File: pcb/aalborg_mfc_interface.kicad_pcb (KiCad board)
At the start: 2 copper layers, 118.1 x 54.6 mm, 27 parts, among them J1 DB15FV, J2 DB15FV, J3 DB15FV, P1 PWR_JACK_2.5x5.5, P2 HEADER_01X03, P3 HEADER_01X03, P4 HEADER_01X03, P5 HEADER_01X03, SW1 SPST_SERIES_M, U1 MAX6817

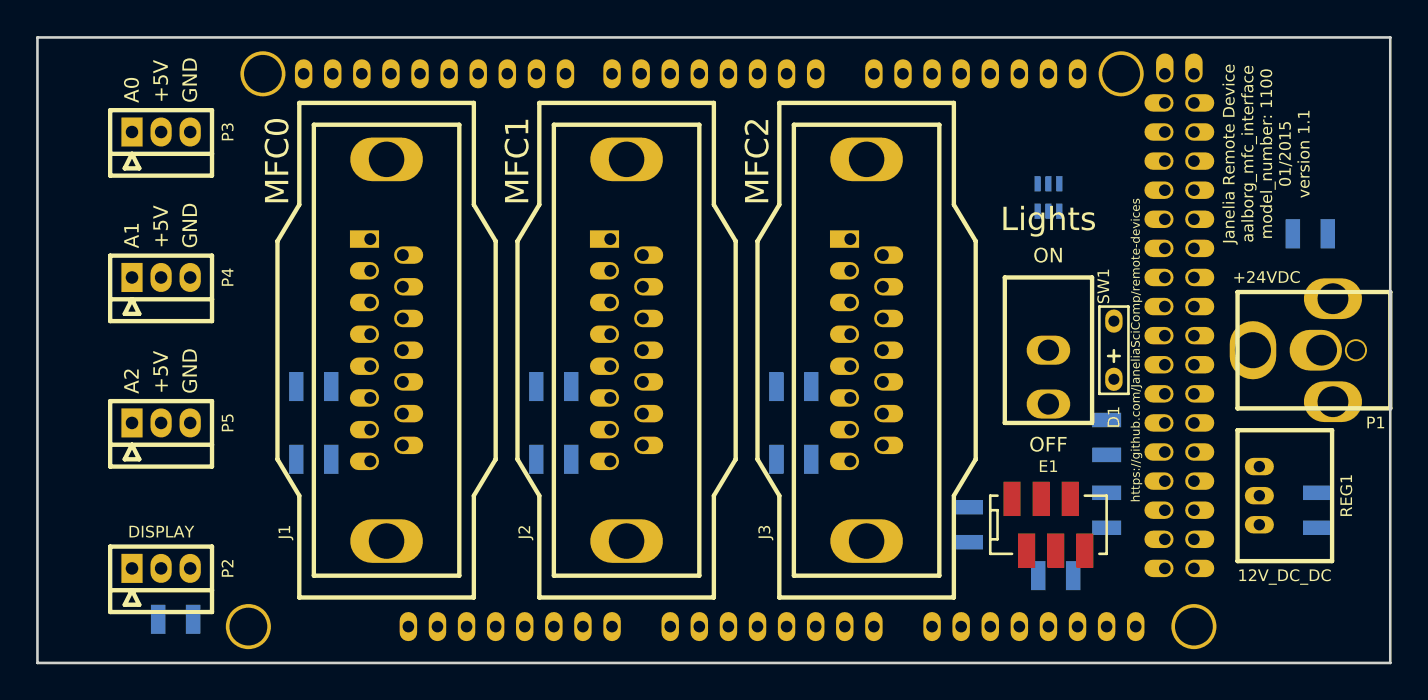
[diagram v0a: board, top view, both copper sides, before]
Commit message: Progress on pcb 1.1 design and firmware 1.0.
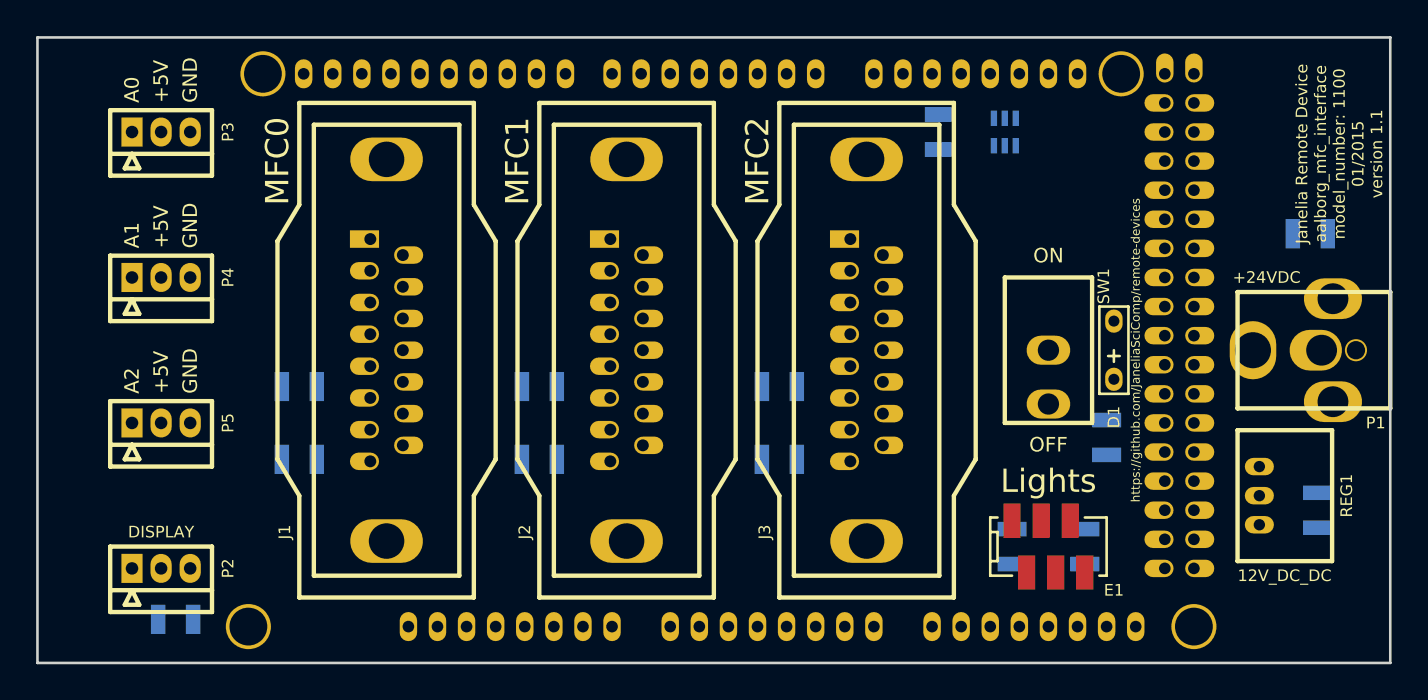
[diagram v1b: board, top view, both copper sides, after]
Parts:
- moved C4 40.0 mm to (172.1, 83.8), turned to 270 degrees
- moved U1 6.87 mm to (177.8, 83.8)
- moved R2 4.26 mm to (178.4, 120.0)
- moved R1 3.70 mm to (184.8, 120.0)
- moved E1 1.91 mm to (181.6, 120.0)
- moved C6 1.27 mm to (137.2, 106.0)
- moved R5 1.27 mm to (137.2, 112.4)
- moved C5 1.27 mm to (116.2, 106.0)
- moved R4 1.27 mm to (116.2, 112.4)
- moved C7 1.27 mm to (158.1, 106.0)
- moved R6 1.27 mm to (158.1, 112.4)
- turned R3 to 270 degrees

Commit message: Progress towards pcb v1.1.
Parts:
- added C8: 10uF, aalborg_mfc_interface:SM1210, B.Cu at (158.1, 106.0)
- added S1: HEADER_01X02, aalborg_mfc_interface:Header_Shrouded_2_Pin, F.Cu at (184.2, 88.3)
- added SW2: KT_SWITCH, aalborg_mfc_interface:KT_SWITCH, F.Cu at (200.0, 88.3)
- added U2: MAX6817, aalborg_mfc_interface:MAX6817, B.Cu at (182.9, 83.2)
- C5: value 10uF -> 0.1uF
- P2: footprint aalborg_mfc_interface:Header_Shrouded_3_Pin -> aalborg_mfc_interface:Header_3_Pin
- P3, P4, P5: value HEADER_01X03 -> HEADER_01X03_SHR
- moved C5 87.8 mm to (200.0, 80.0), turned to 0 degrees
- moved C7 21.0 mm to (137.2, 106.0)
- moved C6 21.0 mm to (116.2, 106.0)
- moved C4 0.90 mm to (172.7, 83.2)
- moved U1 0.63 mm to (177.8, 83.2)
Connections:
- ARDUINO1 pad 20: (no net) -> /D_D20
- ARDUINO1 pad 21: (no net) -> /D_D21
- ARDUINO1 pad 5V_4: (no net) -> +5VD
- C4 pad 1: +5V -> +5VD
- C5 pad 1: /ANALOG_OUT_0 -> +5VD
- C6 pad 1: /ANALOG_OUT_1 -> /ANALOG_OUT_0
- C7 pad 1: /ANALOG_OUT_2 -> /ANALOG_OUT_1
- U1 pad 5: +5V -> +5VD
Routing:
- net GND: track 0.00 -> 395.0 mm
- net +5V: track 0.00 -> 154.4 mm, vias 0 -> 1
- net VAA: track 0.00 -> 138.3 mm, vias 0 -> 1
- net /TX3: track 0.00 -> 111.6 mm
- net /ENC_A: track 0.00 -> 97.7 mm, vias 0 -> 1
- net /PURGE_0: track 0.00 -> 78.6 mm
- net /VALVE_OFF_0: track 0.00 -> 78.2 mm
- net /A1: track 0.00 -> 73.7 mm
- net /A0: track 0.00 -> 73.4 mm
- net /V_IN: track 0.00 -> 71.5 mm
- net /ENC_B: track 0.00 -> 68.7 mm, vias 0 -> 1
- net /A2: track 0.00 -> 61.9 mm
- net /ANALOG_IN_0: track 0.00 -> 60.9 mm
- net /VALVE_OFF_1: track 0.00 -> 56.3 mm
- net /PURGE_1: track 0.00 -> 55.7 mm
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- added copper zone on B.Cu, net GND
- added copper zone on F.Cu, net VAA
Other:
- net class LED_POWER added: clearance 0.254, trace_width 0.6096, via_dia 0.889, via_drill 0.635
- board text added: "IN"

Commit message: Minor changes to names.
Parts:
- S1: value HEADER_01X02 -> HEADER_01X02_SHR
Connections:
- net /D20 renamed /IN
- net /D21 renamed /BTN
- net /D_D20 renamed /D_IN
- net /D_D21 renamed /D_BTN

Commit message: remote -> modular.
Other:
- board text added: "Janelia Modular Device aalborg_mfc_interface model_number: 1100 01/2015 version 1.1"
- board text added: "https://github.com/JaneliaSciComp/modular-devices"
- board text removed: "Janelia Remote Device aalborg_mfc_interface model_number: 1100 01/2015 version 1.1"
- board text removed: "https://github.com/JaneliaSciComp/remote-devices"
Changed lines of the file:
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@@
     (effects (font (size 1.016 1.016) (thickness 0.254)))
   )
-  (gr_text https://github.com/JaneliaSciComp/remote-devices (at 189.23 102.87 90) (layer F.SilkS)
+  (gr_text https://github.com/JaneliaSciComp/modular-devices (at 189.23 102.87 90) (layer F.SilkS)
     (effects (font (size 0.762 0.762) (thickness 0.1905)))
   )
-  (gr_text "Janelia Remote Device\naalborg_mfc_interface\nmodel_number: 1100\n01/2015 version 1.1" (at 207.01 85.725 90) (layer F.SilkS)
+  (gr_text "Janelia Modular Device\naalborg_mfc_interface\nmodel_number: 1100\n01/2015 version 1.1" (at 207.01 85.725 90) (layer F.SilkS)
     (effects (font (size 1.016 1.016) (thickness 0.254)))
   )

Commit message: Finished pcb v1.2.
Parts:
- added P6: HEADER_01X03_SHR, aalborg_mfc_interface:Header_Shrouded_3_Pin, F.Cu at (104.1, 114.9)
- P3: value HEADER_01X03_SHR -> BNC_DOUBLE_RA; footprint aalborg_mfc_interface:Header_Shrouded_3_Pin -> aalborg_mfc_interface:BNC_DOUBLE
- moved P5 20.3 mm to (104.1, 88.9)
- moved P3 19.7 mm to (99.1, 102.9), turned to 90 degrees
- moved P4 15.9 mm to (104.1, 80.6)
- moved P2 1.27 mm to (104.1, 123.2)
- moved C3 0.64 mm to (105.4, 127.0)
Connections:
- net /A0 renamed /BNC_A
- net /A1 renamed /AIN_0
- net /A2 renamed /AIN_1
- net /D_IN renamed /D_SWITCH
- net /IN renamed /SWITCH
- ARDUINO1 pad 17: (no net) -> /D_LED_PWR
- ARDUINO1 pad 18: /D_LED_PWR -> /ENC_A
- ARDUINO1 pad 2: /ENC_A -> /ENC_B
- ARDUINO1 pad 3: /ENC_B -> /BNC_B
- ARDUINO1 pad A3: /ANALOG_IN_0 -> /AIN_2
- ARDUINO1 pad A4: /ANALOG_IN_1 -> /ANALOG_IN_0
- ARDUINO1 pad A5: /ANALOG_IN_2 -> /ANALOG_IN_1
- ARDUINO1 pad A6: (no net) -> /ANALOG_IN_2
- P3 pad 2: +5V -> GND
- P3 pad 3: GND -> /BNC_B
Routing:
- net /AIN_2: track 0.00 -> 70.1 mm
- net /BNC_B: track 0.00 -> 56.7 mm
- net /ENC_A: track 97.7 -> 46.8 mm
- net VAA: track 138.3 -> 169.9 mm, vias 1 -> 4
- net /AIN_0: track 73.7 -> 101.9 mm
- net /TX3: track 111.6 -> 89.6 mm
- net /AIN_1: track 61.9 -> 80.3 mm
- net /PWM_0: track 50.5 -> 66.8 mm, vias 1 -> 0
- net /BNC_A: track 73.4 -> 58.5 mm
- net GND: track 395.0 -> 405.9 mm, vias 0 -> 2
- net +5V: track 154.4 -> 144.9 mm, vias 1 -> 3
- net /D_LED_PWR: track 3.38 -> 10.4 mm
- net /PURGE_1: track 55.7 -> 62.2 mm
- net /ENC_B: track 68.7 -> 63.4 mm, vias 1 -> 2
- net /ANALOG_IN_1: track 39.2 -> 44.1 mm
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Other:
- board text added: "AIN0"
- board text added: "AIN1"
- board text added: "AIN2"
- board text added: "Janelia Modular Device aalborg_mfc_interface model_number: 1100 02/2015 version 1.2"
- board text added: "SWITCH"
- board text removed: "A0"
- board text removed: "A1"
- board text removed: "A2"
- board text removed: "IN"
- board text removed: "Janelia Modular Device aalborg_mfc_interface model_number: 1100 01/2015 version 1.1"

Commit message: JaneliaSciComp -> janelia-modular-devices.
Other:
- board text added: "https://github.com/janelia-modular-devices/modular-devices"
- board text removed: "https://github.com/JaneliaSciComp/modular-devices"
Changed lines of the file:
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@@
     (effects (font (size 1.016 1.016) (thickness 0.254)))
   )
-  (gr_text https://github.com/JaneliaSciComp/modular-devices (at 189.23 102.87 90) (layer F.SilkS)
+  (gr_text https://github.com/janelia-modular-devices/modular-devices (at 189.23 102.87 90) (layer F.SilkS)
     (effects (font (size 0.762 0.762) (thickness 0.1905)))
   )

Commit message: Tiny changes to create v1.3.
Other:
- board text added: "2.5x5.5 Center +"
- board text added: "Janelia Modular Device aalborg_mfc_interface model_number: 1100 08/2015 version 1.3"
- board text added: "https://github.com/janelia-modular-devices"
- board text removed: "Janelia Modular Device aalborg_mfc_interface model_number: 1100 02/2015 version 1.2"
- board text removed: "https://github.com/janelia-modular-devices/modular-devices"
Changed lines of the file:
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@@
-(kicad_pcb (version 4) (host pcbnew 0.201502231246+5447~21~ubuntu14.04.1-product)
+(kicad_pcb (version 4) (host pcbnew 0.201508100901+6080~28~ubuntu14.04.1-product)
   (general
     (links 95)
     (no_connects 0)
-    (area 93.230699 75.450699 211.569301 130.289301)
+    (area 90.995499 74.295 212.725001 131.445001)
     (thickness 1.6)
-    (drawings 22)
+    (drawings 23)
     (tracks 512)
     (zones 0)
@@
   (title_block
     (title aalborg_mfc_interface)
-    (rev 1.2)
+    (rev 1.3)
   )
   (layers
@@
       (net 2 GND))
   )
+  (gr_text "2.5x5.5 Center +" (at 196.85 102.87 90) (layer F.SilkS)
+    (effects (font (size 0.762 0.762) (thickness 0.1905)))
+  )
   (gr_text SWITCH (at 180.975 88.265 90) (layer F.SilkS)
     (effects (font (thickness 0.381)))
@@
     (effects (font (size 1.016 1.016) (thickness 0.254)))
   )
-  (gr_text https://github.com/janelia-modular-devices/modular-devices (at 189.23 102.87 90) (layer F.SilkS)
+  (gr_text https://github.com/janelia-modular-devices (at 189.23 102.87 90) (layer F.SilkS)
     (effects (font (size 0.762 0.762) (thickness 0.1905)))
   )
-  (gr_text "Janelia Modular Device\naalborg_mfc_interface\nmodel_number: 1100\n02/2015 version 1.2" (at 207.01 85.725 90) (layer F.SilkS)
+  (gr_text "Janelia Modular Device\naalborg_mfc_interface\nmodel_number: 1100\n08/2015 version 1.3" (at 207.01 85.725 90) (layer F.SilkS)
     (effects (font (size 1.016 1.016) (thickness 0.254)))
   )

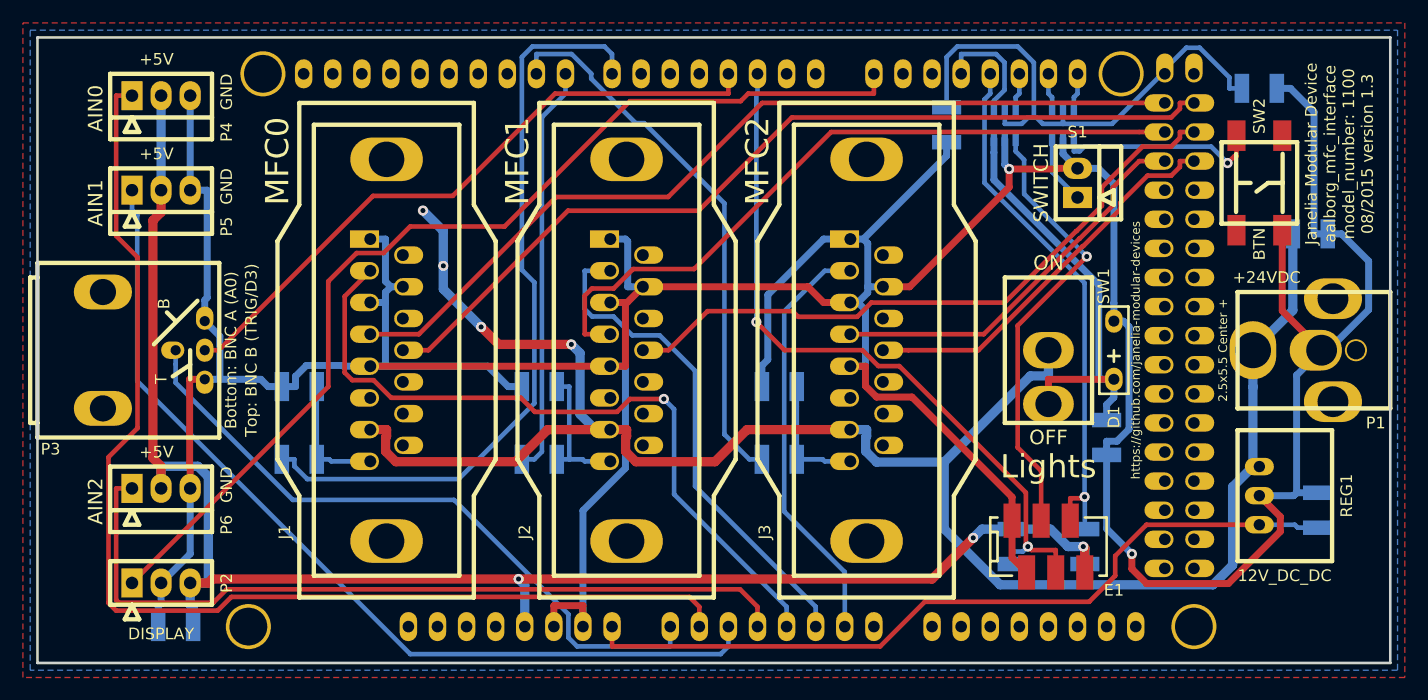
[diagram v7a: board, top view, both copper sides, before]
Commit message: SPST switch -> DPST switch.
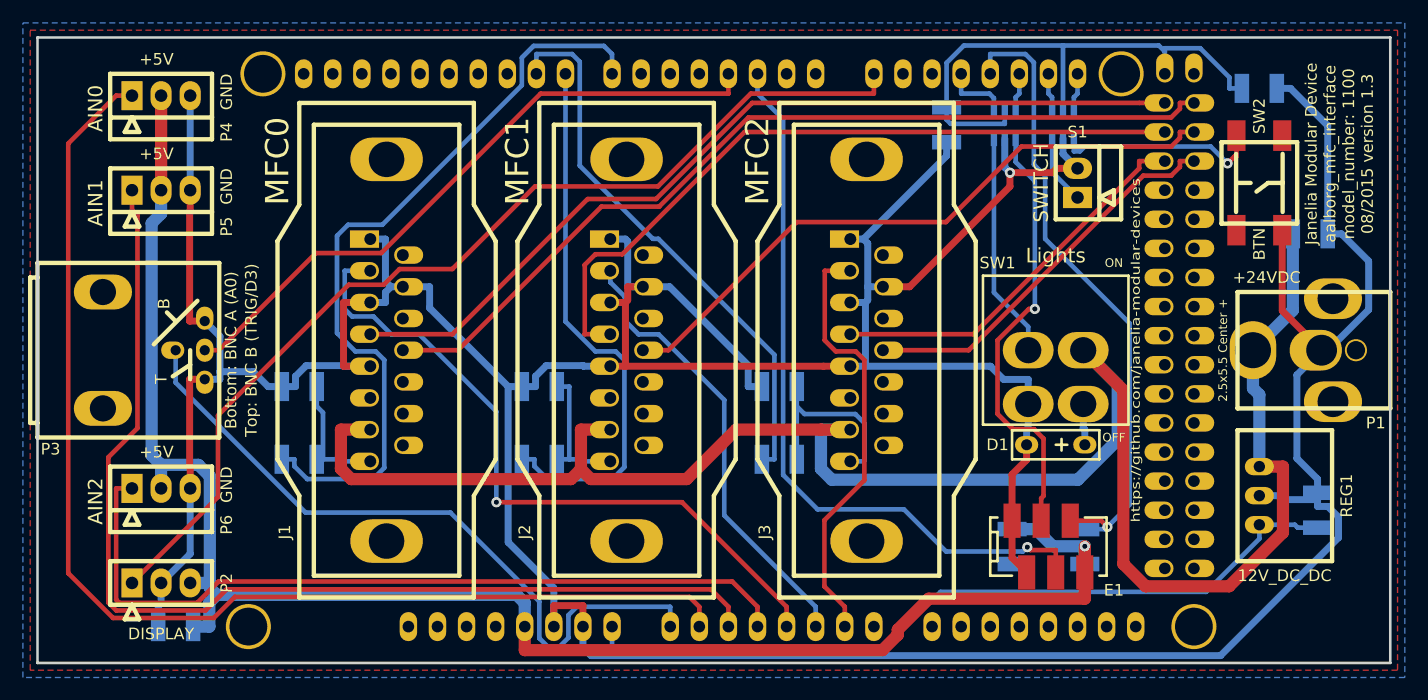
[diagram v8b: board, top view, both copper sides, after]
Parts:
- removed R6: 5.11k, aalborg_mfc_interface:SM1210
- SW1: value SPST_SERIES_M -> DPST_SERIES_M; footprint aalborg_mfc_interface:SPST_SERIES_M -> aalborg_mfc_interface:DPST_SERIES_M
- moved R3 70.5 mm to (116.2, 112.4), turned to 180 degrees
- moved R5 21.0 mm to (158.1, 112.4)
- moved R4 21.0 mm to (137.2, 112.4)
- moved D1 9.69 mm to (182.2, 111.1), turned to 270 degrees
- moved SW1 0.63 mm to (182.2, 102.9)
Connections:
- net /D_LED_PWR renamed /D_LIGHTS
- ARDUINO1 pad 0: (no net) -> Net-(ARDUINO1-Pad0)
- ARDUINO1 pad 1: (no net) -> Net-(ARDUINO1-Pad1)
- ARDUINO1 pad 10: (no net) -> Net-(ARDUINO1-Pad10)
- ARDUINO1 pad 11: (no net) -> Net-(ARDUINO1-Pad11)
- ARDUINO1 pad 12: (no net) -> Net-(ARDUINO1-Pad12)
- ARDUINO1 pad 13: (no net) -> Net-(ARDUINO1-Pad13)
- ARDUINO1 pad 15: (no net) -> Net-(ARDUINO1-Pad15)
- ARDUINO1 pad 16: (no net) -> Net-(ARDUINO1-Pad16)
- ARDUINO1 pad 20B: (no net) -> Net-(ARDUINO1-Pad20B)
- ARDUINO1 pad 21B: (no net) -> Net-(ARDUINO1-Pad21B)
- ARDUINO1 pad 28: (no net) -> Net-(ARDUINO1-Pad28)
- ARDUINO1 pad 29: (no net) -> Net-(ARDUINO1-Pad29)
- ARDUINO1 pad 30: (no net) -> Net-(ARDUINO1-Pad30)
- ARDUINO1 pad 31: (no net) -> Net-(ARDUINO1-Pad31)
- ARDUINO1 pad 32: (no net) -> Net-(ARDUINO1-Pad32)
- ARDUINO1 pad 33: (no net) -> Net-(ARDUINO1-Pad33)
- ARDUINO1 pad 34: (no net) -> Net-(ARDUINO1-Pad34)
- ARDUINO1 pad 35: (no net) -> Net-(ARDUINO1-Pad35)
- ARDUINO1 pad 36: (no net) -> Net-(ARDUINO1-Pad36)
- ARDUINO1 pad 37: (no net) -> Net-(ARDUINO1-Pad37)
- ARDUINO1 pad 38: (no net) -> Net-(ARDUINO1-Pad38)
- ARDUINO1 pad 39: (no net) -> Net-(ARDUINO1-Pad39)
- ARDUINO1 pad 3V3: (no net) -> Net-(ARDUINO1-Pad3V3)
- ARDUINO1 pad 4: (no net) -> Net-(ARDUINO1-Pad4)
- ARDUINO1 pad 40: (no net) -> Net-(ARDUINO1-Pad40)
- ARDUINO1 pad 41: (no net) -> Net-(ARDUINO1-Pad41)
- ARDUINO1 pad 42: (no net) -> Net-(ARDUINO1-Pad42)
- ARDUINO1 pad 43: (no net) -> Net-(ARDUINO1-Pad43)
- ARDUINO1 pad 44: (no net) -> Net-(ARDUINO1-Pad44)
- ARDUINO1 pad 45: (no net) -> Net-(ARDUINO1-Pad45)
- ARDUINO1 pad 46: (no net) -> Net-(ARDUINO1-Pad46)
- ARDUINO1 pad 47: (no net) -> Net-(ARDUINO1-Pad47)
- ARDUINO1 pad 48: (no net) -> Net-(ARDUINO1-Pad48)
- ARDUINO1 pad 49: (no net) -> Net-(ARDUINO1-Pad49)
- ARDUINO1 pad 5: (no net) -> Net-(ARDUINO1-Pad5)
- ARDUINO1 pad 50: (no net) -> Net-(ARDUINO1-Pad50)
- ARDUINO1 pad 51: (no net) -> Net-(ARDUINO1-Pad51)
- ARDUINO1 pad 52: (no net) -> Net-(ARDUINO1-Pad52)
- ARDUINO1 pad 53: (no net) -> Net-(ARDUINO1-Pad53)
- ARDUINO1 pad 5V_5: (no net) -> Net-(ARDUINO1-Pad5V_5)
- ARDUINO1 pad 6: (no net) -> Net-(ARDUINO1-Pad6)
- ARDUINO1 pad A10: (no net) -> Net-(ARDUINO1-PadA10)
- ARDUINO1 pad A11: (no net) -> Net-(ARDUINO1-PadA11)
- ARDUINO1 pad A12: (no net) -> Net-(ARDUINO1-PadA12)
- ARDUINO1 pad A13: (no net) -> Net-(ARDUINO1-PadA13)
- ARDUINO1 pad A14: (no net) -> Net-(ARDUINO1-PadA14)
- ARDUINO1 pad A15: (no net) -> Net-(ARDUINO1-PadA15)
- ARDUINO1 pad A7: (no net) -> Net-(ARDUINO1-PadA7)
- ARDUINO1 pad A8: (no net) -> Net-(ARDUINO1-PadA8)
- ARDUINO1 pad A9: (no net) -> Net-(ARDUINO1-PadA9)
- ARDUINO1 pad AREF: (no net) -> Net-(ARDUINO1-PadAREF)
- ARDUINO1 pad GND3: (no net) -> Net-(ARDUINO1-PadGND3)
- ARDUINO1 pad GND4: (no net) -> Net-(ARDUINO1-PadGND4)
- ARDUINO1 pad GND5: (no net) -> Net-(ARDUINO1-PadGND5)
- ARDUINO1 pad IREF: (no net) -> Net-(ARDUINO1-PadIREF)
- ARDUINO1 pad NC: (no net) -> Net-(ARDUINO1-PadNC)
- ARDUINO1 pad RST: (no net) -> Net-(ARDUINO1-PadRST)
- J1 pad 11: (no net) -> Net-(J1-Pad11)
- J1 pad 13: (no net) -> Net-(J1-Pad13)
- J1 pad 14: (no net) -> Net-(J1-Pad14)
- J1 pad 15: (no net) -> Net-(J1-Pad15)
- J1 pad 6: (no net) -> Net-(J1-Pad6)
- J1 pad 9: (no net) -> Net-(J1-Pad9)
- J2 pad 11: (no net) -> Net-(J2-Pad11)
- J2 pad 13: (no net) -> Net-(J2-Pad13)
- J2 pad 14: (no net) -> Net-(J2-Pad14)
- J2 pad 15: (no net) -> Net-(J2-Pad15)
- J2 pad 6: (no net) -> Net-(J2-Pad6)
- J2 pad 9: (no net) -> Net-(J2-Pad9)
- J3 pad 11: (no net) -> Net-(J3-Pad11)
- J3 pad 13: (no net) -> Net-(J3-Pad13)
- J3 pad 14: (no net) -> Net-(J3-Pad14)
- J3 pad 15: (no net) -> Net-(J3-Pad15)
- J3 pad 6: (no net) -> Net-(J3-Pad6)
- J3 pad 9: (no net) -> Net-(J3-Pad9)
- R3 pad 1: /LED_PWR -> /ANALOG_OUT_0
- R3 pad 2: GND -> /PWM_0
- R4 pad 1: /ANALOG_OUT_0 -> /ANALOG_OUT_1
- R4 pad 2: /PWM_0 -> /PWM_1
- R5 pad 1: /ANALOG_OUT_1 -> /ANALOG_OUT_2
- R5 pad 2: /PWM_1 -> /PWM_2
- U1 pad 3: /LED_PWR -> /LIGHTS
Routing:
- net /LED_PWR: track 37.8 -> 3.64 mm
- net /LIGHTS: track 0.00 -> 19.7 mm
- net /AIN_1: track 80.3 -> 94.8 mm
- net GND: track 405.9 -> 419.7 mm, vias 2 -> 1
- net /PWM_1: track 35.9 -> 48.0 mm
- net /ENC_A: track 46.8 -> 56.2 mm
- net +5V: track 144.9 -> 151.8 mm, vias 3 -> 1
- net /ANALOG_OUT_2: track 11.1 -> 17.4 mm
- net /ANALOG_IN_1: track 44.1 -> 39.5 mm
- net /D_LIGHTS: track 10.4 -> 5.87 mm
- net /BNC_A: track 58.5 -> 61.8 mm
- net /ANALOG_IN_0: track 63.9 -> 61.3 mm
- net /ENC_B: track 63.4 -> 65.8 mm, vias 2 -> 1
- net /AIN_0: track 101.9 -> 104.4 mm
- net +5VD: track 46.2 -> 47.9 mm
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- added copper zone on F.Cu, net GND
- removed copper zone on F.Cu, net VAA
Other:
- net class POWER: trace_width 0.8128 -> 1.0668
